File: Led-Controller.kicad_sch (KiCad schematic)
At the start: 107 parts, among them J1 Program, J2 Barrel_Jack, J3 Screw_Terminal, J4 Screw_Terminal, J5 Ws2812 Conn, J6 Screw_Terminal, Q1 CSD18540Q5B, Q2 CSD18540Q5B, Q3 CSD18540Q5B, Q4 CSD18540Q5B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

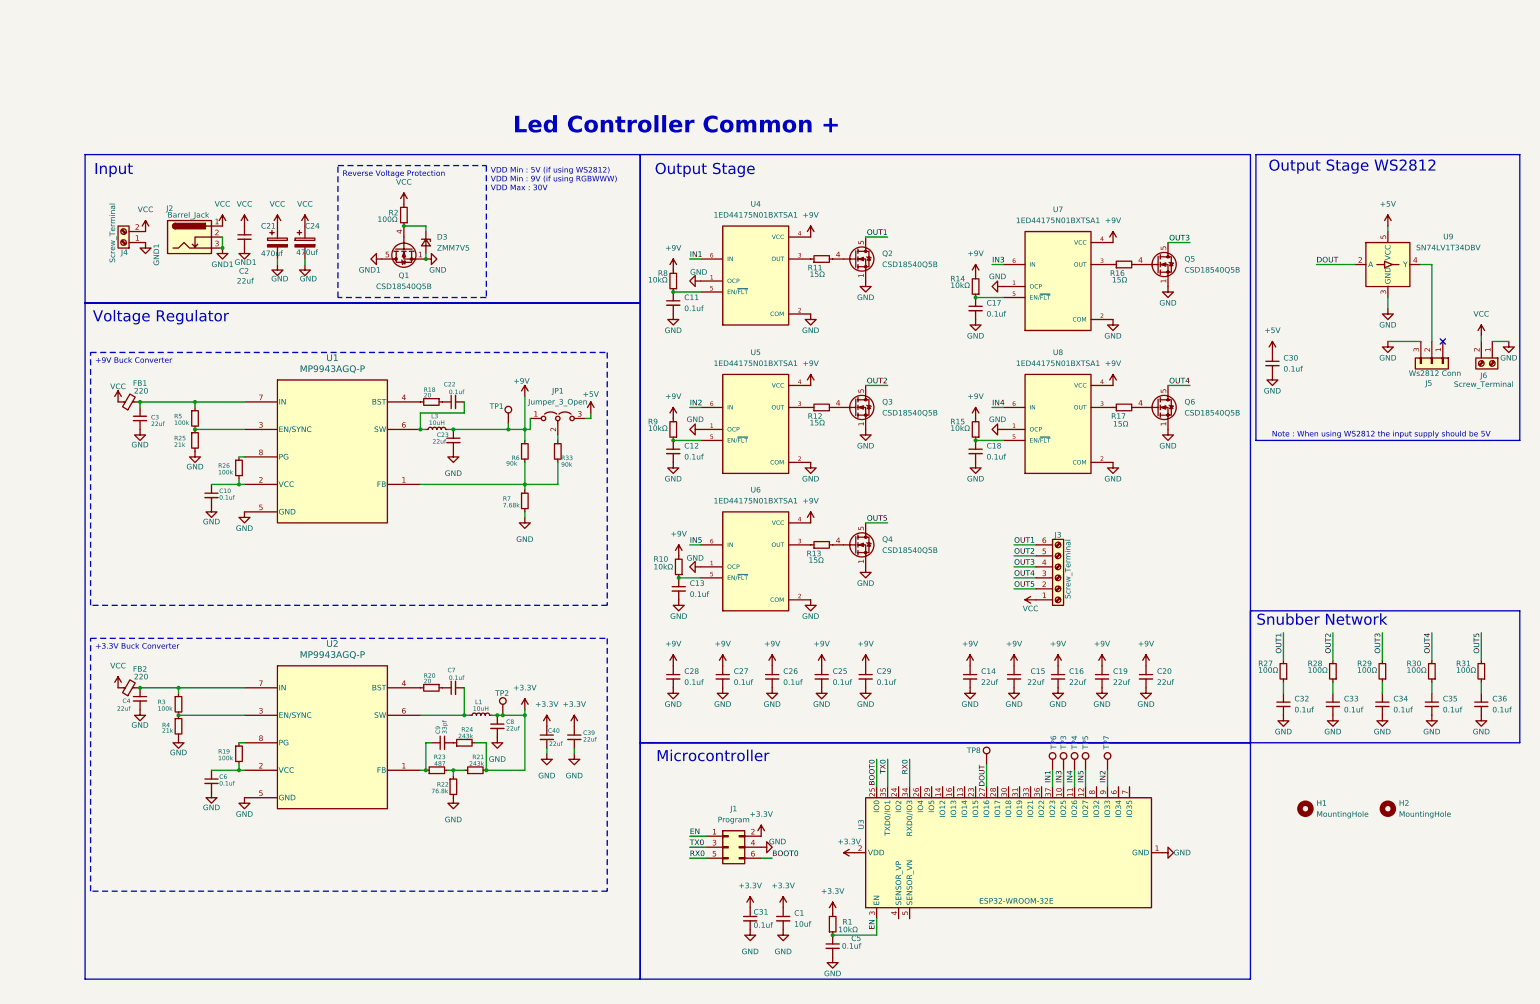
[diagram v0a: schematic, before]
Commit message: Added: Bare ESP32 Chip
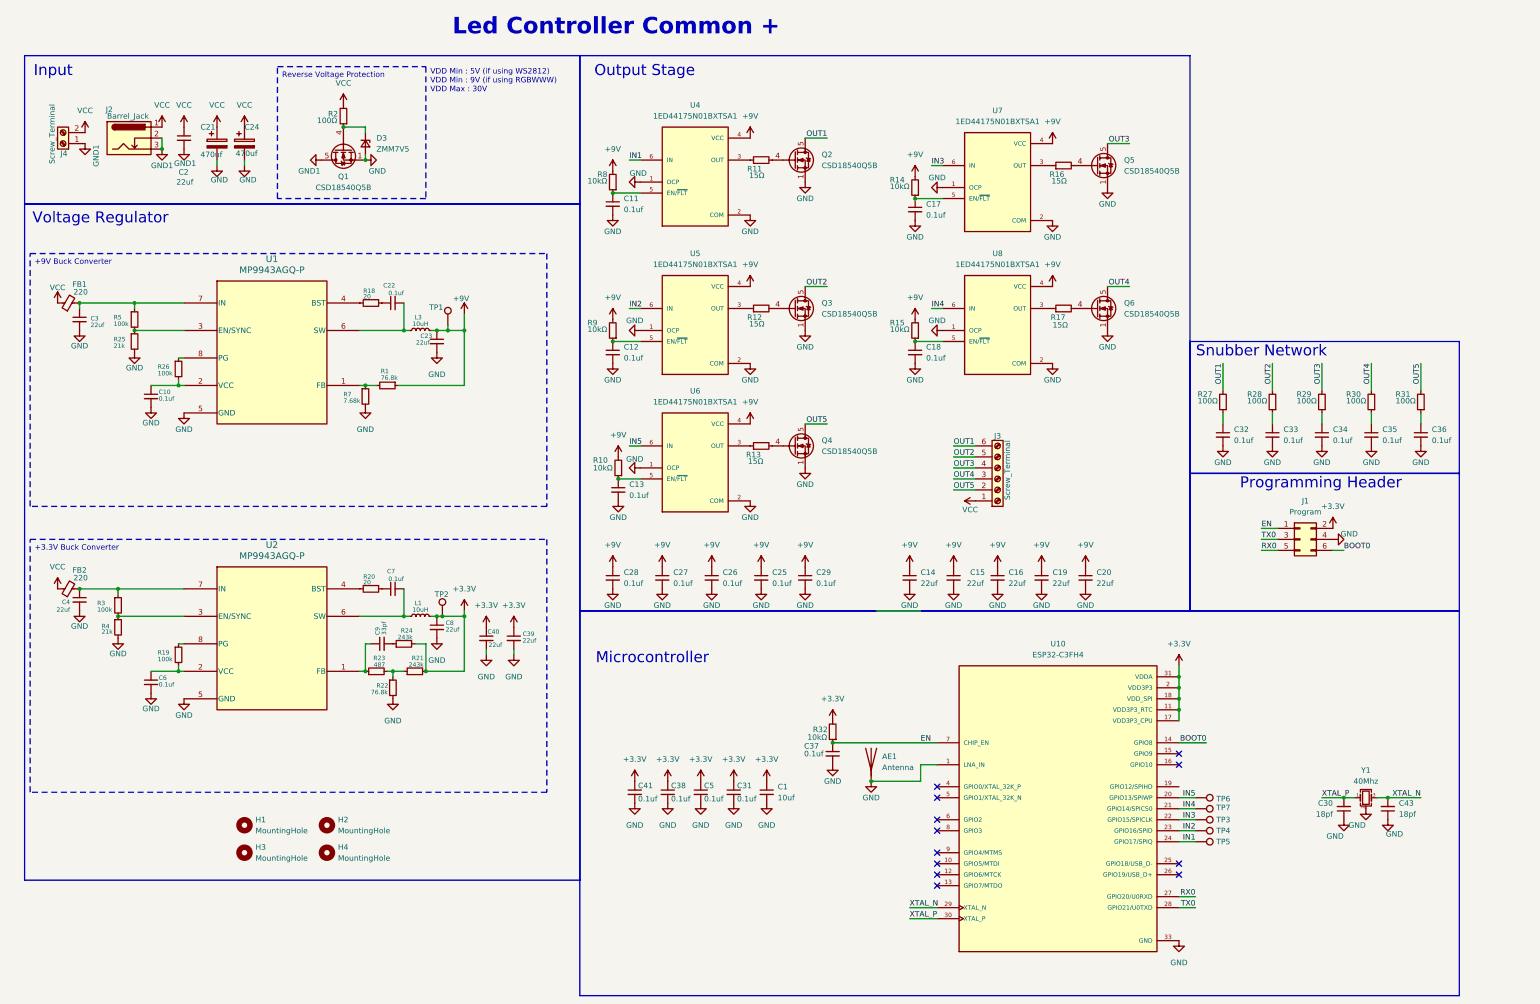
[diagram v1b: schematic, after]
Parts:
- removed J5: Ws2812 Conn, Connector_PinHeader_2.54mm:PinHeader_1x03_P2.54mm_Horizontal, symbol Connector_Generic:Conn_01x03
- removed J6: Screw_Terminal, TerminalBlock:TerminalBlock_bornier-2_P5.08mm, symbol Connector:Screw_Terminal_01x02
- removed JP1: Jumper_3_Open, Jumper:SolderJumper-3_P2.0mm_Open_TrianglePad1.0x1.5mm, symbol Jumper:Jumper_3_Open
- removed R33, R6: 90k, Resistor_SMD:R_0603_1608Metric, symbol Device:R_Small
- removed TP8: ~, TestPoint:TestPoint_Pad_D1.0mm, symbol Connector:TestPoint
- removed U3: ESP32-WROOM-32E, RF_Module:ESP32-WROOM-32D, symbol RF_Module:ESP32-WROOM-32E
- removed U9: SN74LV1T34DBV, Package_TO_SOT_SMD:SOT-23-5, symbol Logic_LevelTranslator:SN74LV1T34DBV
- added AE1: Antenna, symbol Device:Antenna
- added C37, C38, C41: 0.1uf, Capacitor_SMD:C_0603_1608Metric, symbol Device:C_Small
- added C43: 18pf, Capacitor_SMD:C_0603_1608Metric, symbol Device:C_Small
- added H3, H4: MountingHole, MountingHole:MountingHole_3.2mm_M3_DIN965_Pad, symbol Mechanical:MountingHole
- added R32: 10kΩ, Resistor_SMD:R_0603_1608Metric, symbol Device:R_Small
- added U10: ESP32-C3FH4, ESP32-C3FH4:QFN50P500X500X90-33N, symbol ESP32-C3FH4:ESP32-C3FH4
- added Y1: 40Mhz, Crystal:Crystal_SMD_2016-4Pin_2.0x1.6mm, symbol Device:Crystal_GND24_Small
- C30: value 0.1uf -> 18pf; footprint Capacitor_SMD:C_0805_2012Metric -> Capacitor_SMD:C_0603_1608Metric; Package 805 -> 402; Part No GCM21BR71E104KA37L -> (none)
- R1: value 10kΩ -> 76.8k; Part No RC0603FR-0710KL -> RC0603FR-0776K8L
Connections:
- net +5V is gone; now on net GND: C30.1
- net +3.3V: now also C5.1, C38.1, C41.1, R32.2, U10.11 (VDD3P3_RTC), U10.17 (VDD3P3_CPU), U10.18 (VDD_SPI), U10.2 (VDD3P3), U10.3 (VDD3P3), U10.31 (VDDA), U10.32 (VDDA); no longer R1.2
- net +9V: now also R1.1
- net BOOT0: now also U10.14 (GPIO8)
- net EN: now also C37.1, R32.1, U10.7 (CHIP_EN); no longer C5.1, R1.1
- net GND: now also AE1.1 (A), C37.2, C38.2, C41.2, C43.1, U10.1 (LNA_IN), U10.33 (GND), Y1.2 (G), Y1.4 (G); no longer C30.2
- net IN1: now also TP5.1, U10.24 (GPIO17/SPIQ); no longer TP6.1
- net IN2: now also TP4.1, U10.23 (GPIO16/SPID); no longer TP7.1
- net IN3: now also U10.22 (GPIO15/SPICLK)
- net IN4: now also TP7.1, U10.21 (GPIO14/SPICS0); no longer TP4.1
- net IN5: now also TP6.1, U10.20 (GPIO13/SPIWP); no longer TP5.1
- net RX0: now also U10.27 (GPIO20/U0RXD)
- net TX0: now also U10.28 (GPIO21/U0TXD)
- net at R7.1, U1.1 (FB): now also R1.2
- new net XTAL_N: C43.2, U10.29 (XTAL_N), Y1.3
- new net XTAL_P: C30.2, U10.30 (XTAL_P), Y1.1
- no-connect marks 1 -> 12
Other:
- note added: "Programming Header"
- note removed: "Note : When using WS2812 the input supply should be 5V"
- note removed: "Output Stage WS2812"
- moved on the sheet: C1, C10, C11, C12, C13, C14, C15, C16, C17, C18, C19, C2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
